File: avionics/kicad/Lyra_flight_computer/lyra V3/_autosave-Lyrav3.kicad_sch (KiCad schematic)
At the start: 91 parts, among them J1 USB_B_Micro, J12 Conn_02x03_Odd_Even, J13 Conn_02x03_Odd_Even, J14 Conn_01x04, J15 Conn_01x04, J16 Conn_01x03, J18 1862372, J2 1862372, J3 Conn_01x03, J4 Conn_01x02, J6 Conn_02x03_Odd_Even, Q1 AO3401A, Q2 BSS138, Q3 BSS138, U1 AMS1117-5.0, U10 MPL3115A2, U2 HXY9926S, U3 LIS3MDL, U4 ADXL375BCCZ-RL7, U5 W25Q128JVS, U6 RP2040, U7 BMI088, U8 AMS1117-3.3, U9 HXY9926S, X2 S3D12.288000B20F30T

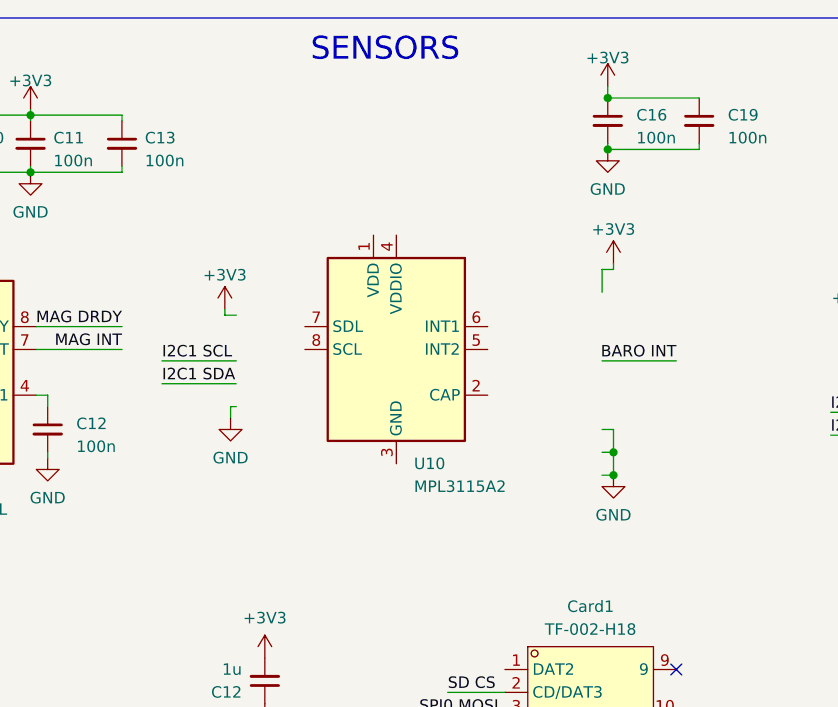
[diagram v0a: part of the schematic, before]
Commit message: lyra v3 work
got most of the sensors and other stuff picked out
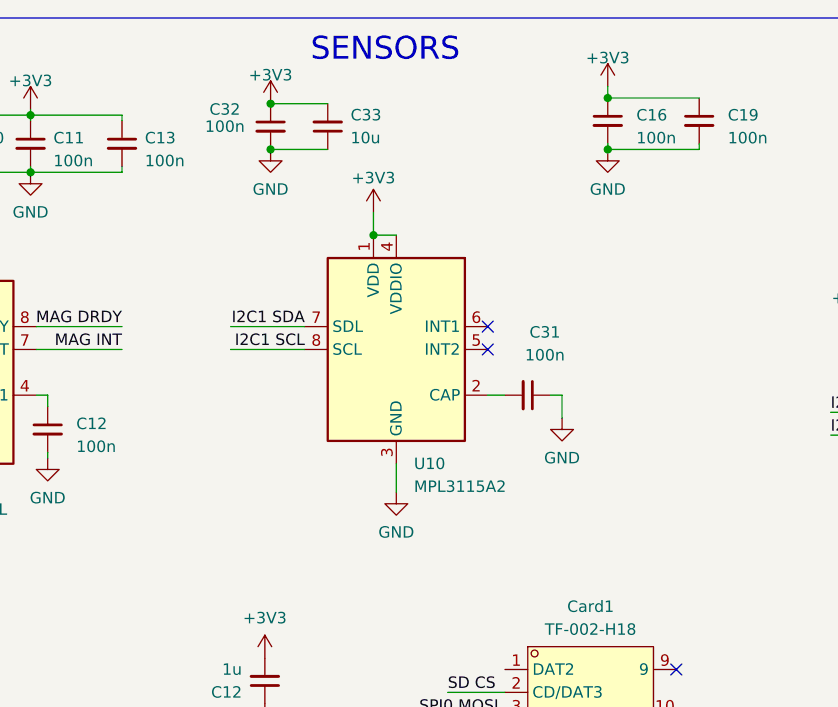
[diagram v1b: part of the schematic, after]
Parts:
- added C31, C32: 100n, Capacitor_SMD:C_0603_1608Metric, symbol Device:C_Small
- added C33: 10u, Capacitor_SMD:C_0603_1608Metric, symbol Device:C_Small
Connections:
- net +3V3: now also U10.1 (VDD), U10.4 (VDDIO), C32.1, C33.2
- net GND: now also U10.3 (GND), C31.1, C32.2, C33.1
- net I2C1 SCL: now also U10.8 (SCL)
- net I2C1 SDA: now also U10.7 (SDL)
- net at U10.2 (CAP): now also C31.2
- no-connect marks 12 -> 14

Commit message: lyrav3 work and more orientation work
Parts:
- removed U2: HXY9926S, easyeda2kicad:SOP-8_L4.9-W3.9-P1.27-LS6.0-BL, symbol easyeda2kicad:HXY9926S
- added Q4: Q_Dual_NMOS_S1G1S2G2D2D2D1D1, easyeda2kicad:SOP-8_L4.9-W3.9-P1.27-LS6.0-BL, symbol Device:Q_Dual_NMOS_S1G1S2G2D2D2D1D1
- C1, C4, C5, C6: footprint Capacitor_SMD:C_0805_2012Metric -> Capacitor_SMD:C_0603_1608Metric
- C10, C11, C12, C13, C15, C16, C17, C18, C20, C21, C22, C23, C24, C25, C26, C27, C28, C29, C3, C30, C31, C9: footprint Capacitor_SMD:C_0603_1608Metric -> (none)
- C19: value 100n -> 10u; footprint Capacitor_SMD:C_0603_1608Metric -> (none)
- C2, C7, C8: footprint Capacitor_SMD:C_0805_2012Metric -> (none)
- C32: value 100n -> 1u; footprint Capacitor_SMD:C_0603_1608Metric -> (none)
- C33: value 10u -> 100n; footprint Capacitor_SMD:C_0603_1608Metric -> (none)
- D1: footprint Diode_SMD:D_0805_2012Metric -> (none)
- D2: footprint LED_SMD:LED_0805_2012Metric -> (none)
- F1, F2: footprint Fuse:Fuse_1206_3216Metric -> (none)
- FB1: footprint Diode_SMD:D_0603_1608Metric -> (none)
- J14, J15: footprint Connector_PinHeader_2.54mm:PinHeader_1x04_P2.54mm_Vertical -> Connector_JST:JST_SH_SM04B-SRSS-TB_1x04-1MP_P1.00mm_Horizontal
- J3: footprint (none) -> Connector_JST:JST_SH_SM03B-SRSS-TB_1x03-1MP_P1.00mm_Horizontal; LCSC Part (none) -> C160403
- J4: footprint (none) -> Connector_PinHeader_2.54mm:PinHeader_1x02_P2.54mm_Vertical
- J6: footprint Connector_PinHeader_2.54mm:PinHeader_2x03_P2.54mm_Vertical -> Connector_JST:JST_SH_SM06B-SRSS-TB_1x06-1MP_P1.00mm_Horizontal
- R1, R10, R11, R12, R13, R14, R15, R16, R17, R18, R19, R2, R3, R4, R5, R6, R7, R8, R9: footprint Resistor_SMD:R_0603_1608Metric -> (none)
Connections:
- net +12P: now also J18.15 (8.1), J18.16 (8.2)
- net +3V3: now also C31.1, J18.7 (4.1), J18.8 (4.2), U4.1 (VDDI/O), U4.3 (RESERVED), U4.6 (VS), U4.7 (~{CS}); no longer C33.2
- net +5V: now also J18.11 (6.1), J18.12 (6.2)
- net GND: now also C31.2, C33.2, J18.10 (5.2), J18.5 (3.1), J18.6 (3.2), J18.9 (5.1), U4.11 (RESERVED), U4.12 (SDO/ALTADDRESS), U4.2 (GND), U4.4 (GND), U4.5 (GND); no longer C31.1, C33.1
- net I2C1 SCL: now also U4.14 (SCL/SCLK)
- net I2C1 SDA: now also U4.13 (SDA/SDI/SDIO)
- net P1-: now also J2.21 (11.1), J2.22 (11.2)
- net P2-: now also J2.17 (9.1), J2.18 (9.2)
- net PYRO PWR: now also J18.13 (7.1), J18.14 (7.2), J2.11 (6.1), J2.12 (6.2), J2.15 (8.1), J2.16 (8.2), J2.19 (10.1), J2.20 (10.2), J2.23 (12.1), J2.24 (12.2)
- net at U10.2 (CAP): now also C33.1; no longer C31.2
- net at J2.1 (1.1): now also J2.2 (1.2)
- net P4-: now reaches J2.10 (5.2)
- net P4-: now also J2.9 (5.1)
- net P3-: now reaches J2.13 (7.1)
- net P3-: now also J2.14 (7.2)
- net at J2.3 (2.1): now also J2.4 (2.2)
- net at J2.5 (3.1): now also J2.6 (3.2)
- net at J2.7 (4.1): now also J2.8 (4.2)
- net at J18.1 (1.1): now also J18.2 (1.2)
- net at J18.3 (2.1): now also J18.4 (2.2)
- no-connect marks 14 -> 17
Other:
- moved on the sheet: BUZZER1, C1, C10, C11, C12, C13, C15, C16, C17, C18, C19, C2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
